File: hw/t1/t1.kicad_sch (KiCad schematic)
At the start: 65 parts, among them J1 SFP edge (INF-8074i), J2 Rosenberger E6S20A-40MT5-Z (H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, U1 DP83TG720S-Q1 (or DP83TC812S-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, U2 STM32G031F6P6, U3 TPS62822DLC, U4 TPS22918DBVR, Y1 25MHz CL8pF 2016

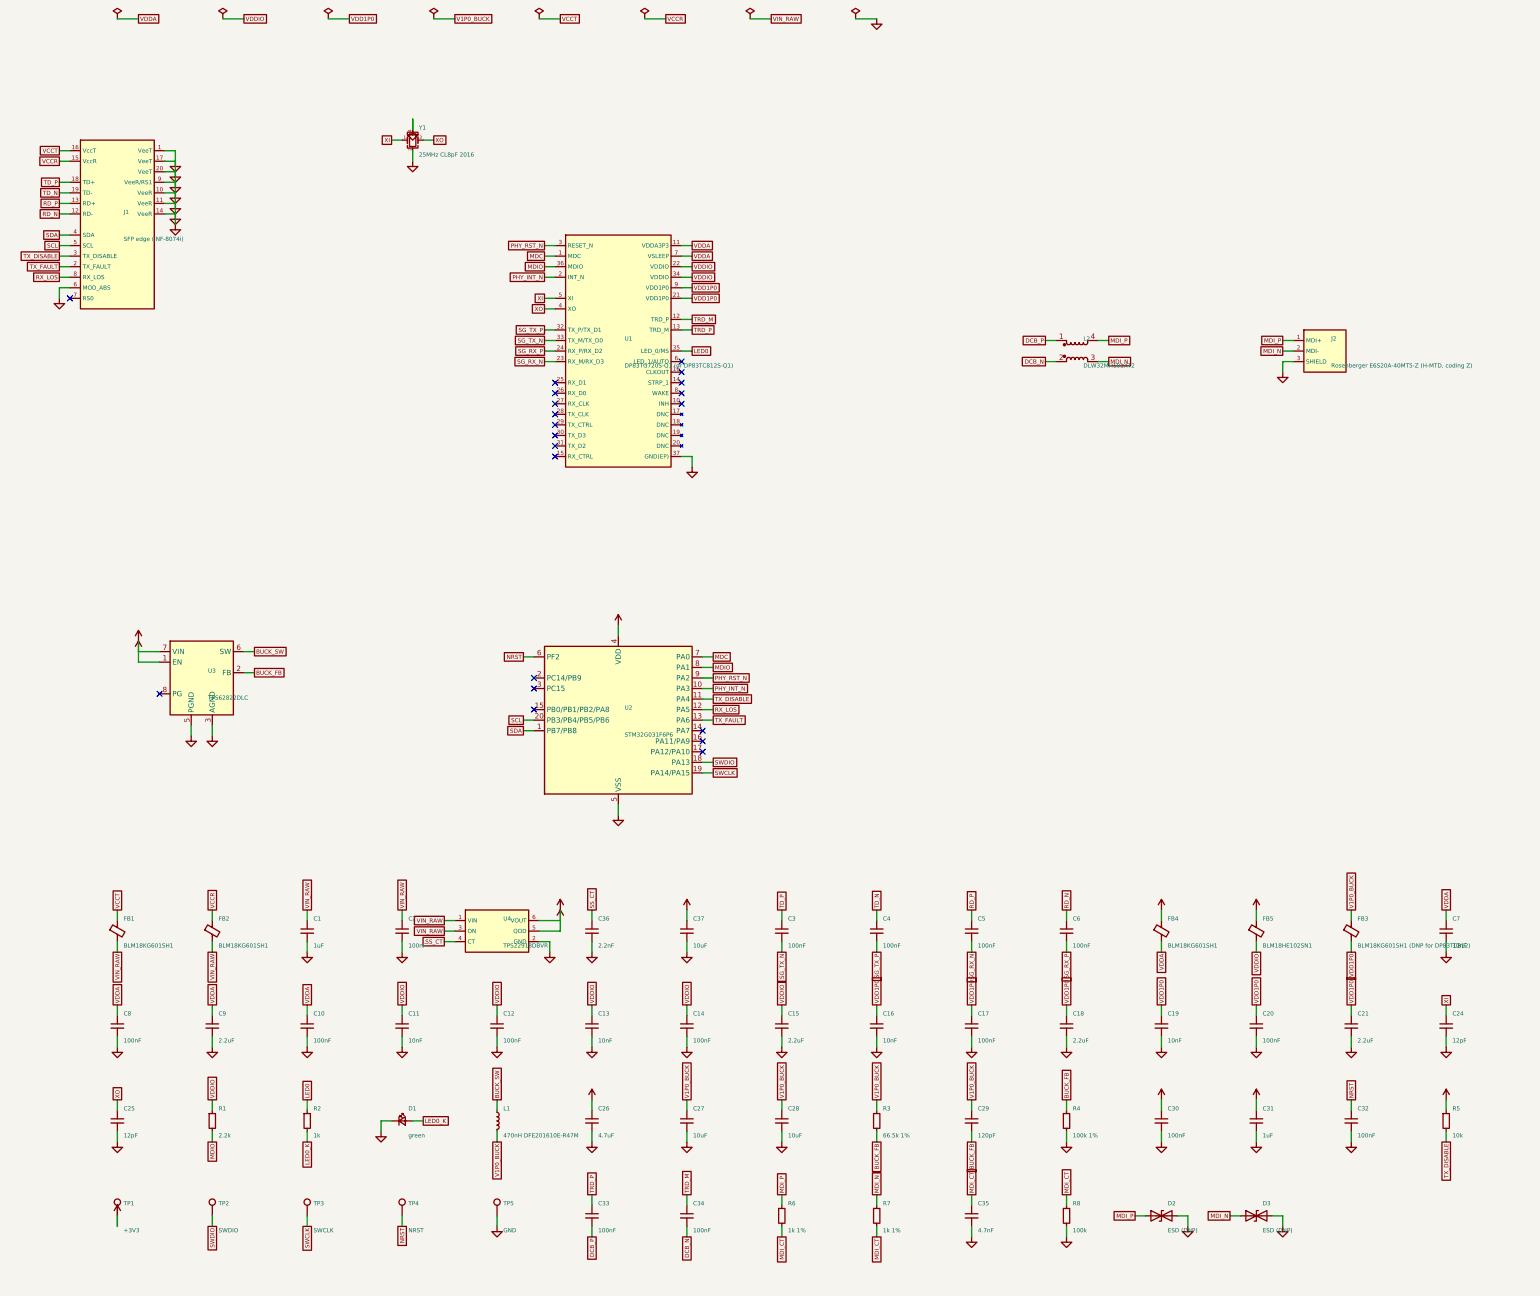
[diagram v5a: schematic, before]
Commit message: T1S: 6-layer board routed and clean, JLC panel and order sheet
- DRC 0 / 0 unconnected (KiCad 7 and 9), schematic parity clean, ERC 0
  errors; gerbers, BOM/CPL, 1:1 print; 5-board panel, DRC clean with the
  board's rules
- the core rail is an In4 island (on In2 it walled the ball field in); In2
  carries two hand-laid buses to the MCU, found once by a maze search and
  baked into make_t1s.py (IN2_BUS)
- JTAG pads beside the FPGA, flash turned 180 degrees, strap/XTO/+3V3 vias in
  the PHY's pads, the MDI pair swapped at the PHY (DME is polarity-free),
  L3/M12 reconnected (they had slipped into a comment)
- MCU pins follow the buses: TX_DISABLE / TX_FAULT on PC14 / PC15 (fw)
- sfpgen: side-pin power stubs no longer turn (GND on TXCLK merged half
  the FPGA's nets in the schematic); ISLANDS as outlines; router vias that
  double a plane dogbone are dropped; T1/RJ45 schematics regenerated,
  both still pass ERC and KiCad 9
- CI: t1s joins the KiCad 9 matrix
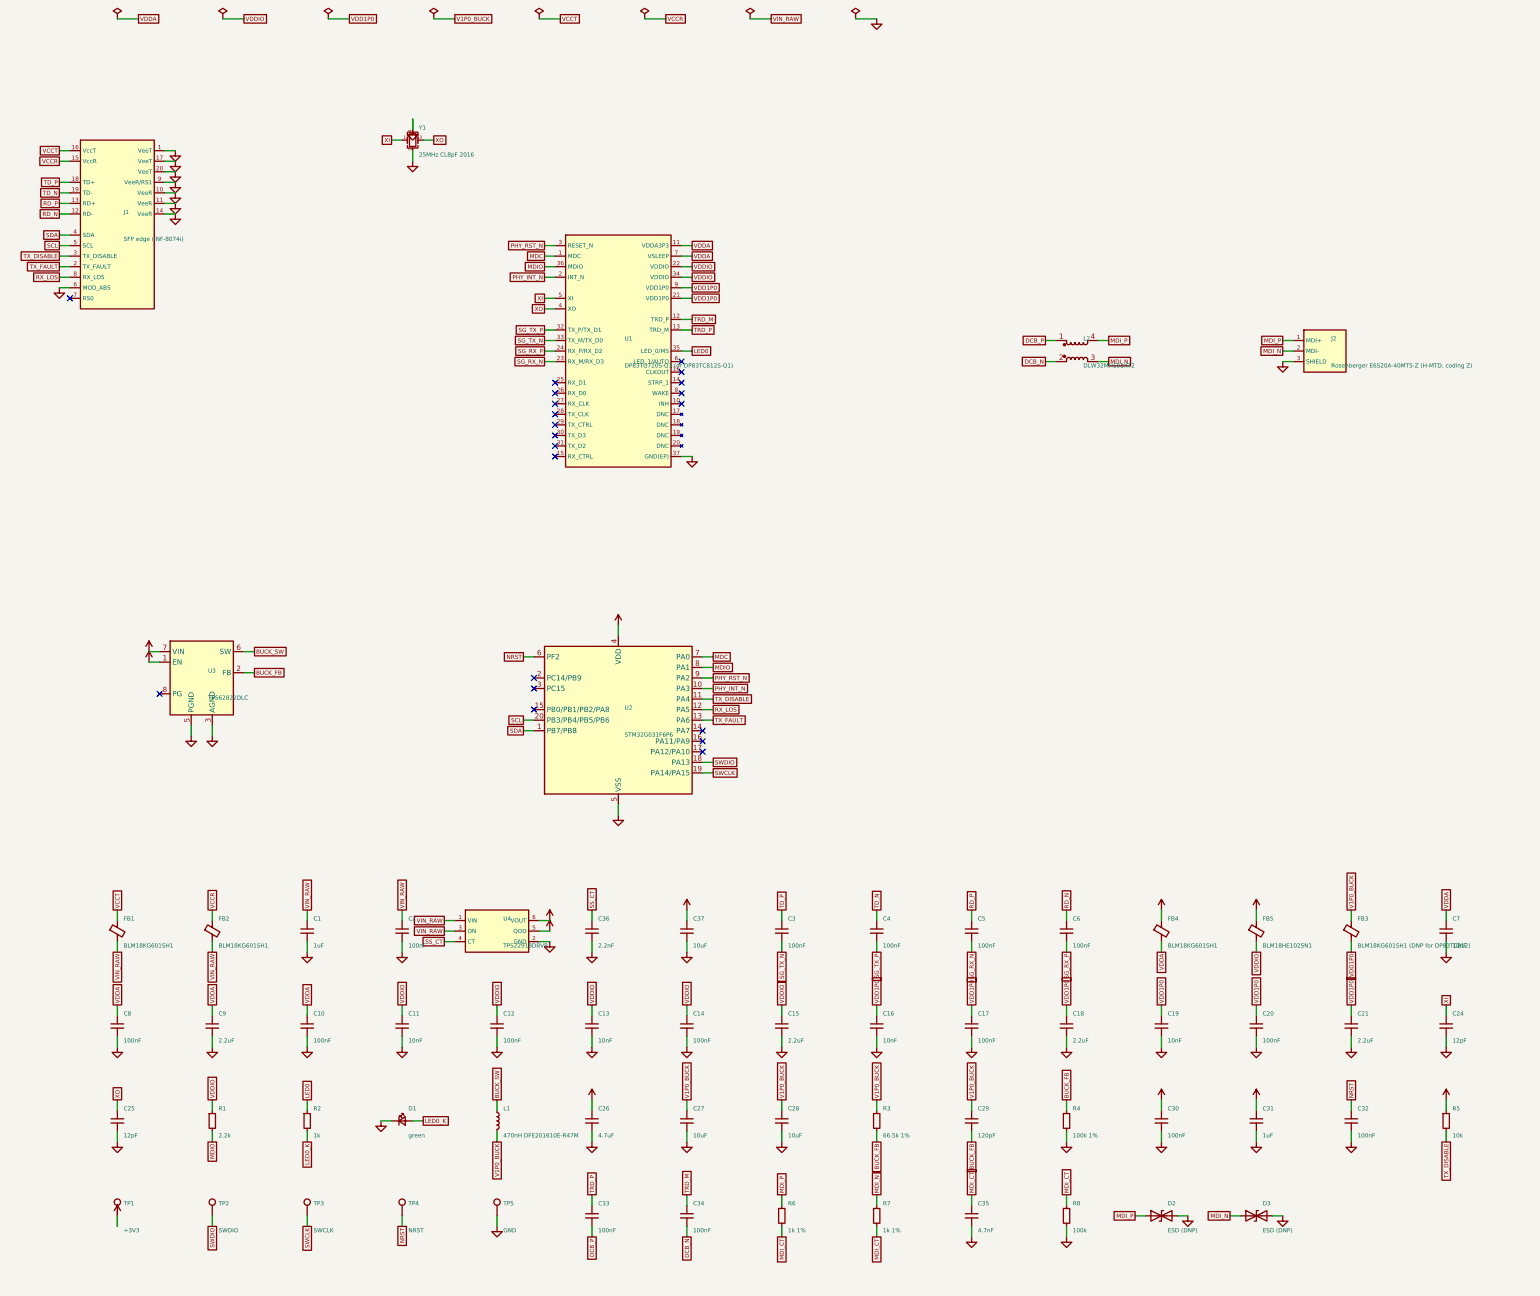
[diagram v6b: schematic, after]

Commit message: Review fixes: 100 V MDI DC block, 128 Mbit flash, T1S MDI geometry
- T1 C33/C34: 100 nF 100 V X5R 0402 (GRM155R62A104KE14D, C162178), split
  from the 16 V decap line (C1525) they had been grouped with
- T1 R6/R7: 1 k 1 % 0.2 W anti-surge 0402 (C313354) instead of 62.5 mW;
  still short of TI's 0.75 W 2010, documented
- T1S U2: GD25Q128EWIGR (C2982923), same WSON-8 footprint, so Gowin's
  default golden address 0x800000 is inside the part; ORDER.md gives the
  flash layout
- compliance.py: each lane's geometry comes from its routed track width;
  the T1S MDI is two 0.2 mm lines (Z0 44.8) with its own delay and loss,
  and an unsolved width now stops the run
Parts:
- C33, C34: value 100nF -> 100nF 100V; LCSC C1525 -> C162178; MPN (none) -> GRM155R62A104KE14D
- R6, R7: value 1k 1% -> 1k 1% 0.2W; LCSC C11702 -> C313354; MPN (none) -> CRCW04021K00FKEDHP
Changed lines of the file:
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@@
     (in_bom yes) (on_board yes) (dnp no)
     (property "Reference" "C33" (at 155.17 315.77 0) (effects (font (size 1.0 1.0)) (justify left)))
-    (property "Value" "100nF" (at 155.17 322.27 0) (effects (font (size 1.0 1.0)) (justify left)))
+    (property "Value" "100nF 100V" (at 155.17 322.27 0) (effects (font (size 1.0 1.0)) (justify left)))
     (property "Footprint" "Capacitor_SMD:C_0402_1005Metric" (at 153.67 318.77 0) (effects (font (size 1.0 1.0)) hide))
     (property "Datasheet" "" (at 153.67 318.77 0) (effects (font (size 1.0 1.0)) hide))
-    (property "LCSC" "C1525" (at 153.67 318.77 0) (effects (font (size 1.0 1.0)) hide))
+    (property "MPN" "GRM155R62A104KE14D" (at 153.67 318.77 0) (effects (font (size 1.0 1.0)) hide))
+    (property "LCSC" "C162178" (at 153.67 318.77 0) (effects (font (size 1.0 1.0)) hide))
     (pin "1")
     (pin "2")
@@
     (in_bom yes) (on_board yes) (dnp no)
     (property "Reference" "C34" (at 178.03 315.77 0) (effects (font (size 1.0 1.0)) (justify left)))
-    (property "Value" "100nF" (at 178.03 322.27 0) (effects (font (size 1.0 1.0)) (justify left)))
+    (property "Value" "100nF 100V" (at 178.03 322.27 0) (effects (font (size 1.0 1.0)) (justify left)))
     (property "Footprint" "Capacitor_SMD:C_0402_1005Metric" (at 176.53 318.77 0) (effects (font (size 1.0 1.0)) hide))
     (property "Datasheet" "" (at 176.53 318.77 0) (effects (font (size 1.0 1.0)) hide))
-    (property "LCSC" "C1525" (at 176.53 318.77 0) (effects (font (size 1.0 1.0)) hide))
+    (property "MPN" "GRM155R62A104KE14D" (at 176.53 318.77 0) (effects (font (size 1.0 1.0)) hide))
+    (property "LCSC" "C162178" (at 176.53 318.77 0) (effects (font (size 1.0 1.0)) hide))
     (pin "1")
     (pin "2")
@@
     (in_bom yes) (on_board yes) (dnp no)
     (property "Reference" "R6" (at 200.89 315.77 0) (effects (font (size 1.0 1.0)) (justify left)))
-    (property "Value" "1k 1%" (at 200.89 322.27 0) (effects (font (size 1.0 1.0)) (justify left)))
+    (property "Value" "1k 1% 0.2W" (at 200.89 322.27 0) (effects (font (size 1.0 1.0)) (justify left)))
     (property "Footprint" "Resistor_SMD:R_0402_1005Metric" (at 199.39 318.77 0) (effects (font (size 1.0 1.0)) hide))
     (property "Datasheet" "" (at 199.39 318.77 0) (effects (font (size 1.0 1.0)) hide))
-    (property "LCSC" "C11702" (at 199.39 318.77 0) (effects (font (size 1.0 1.0)) hide))
+    (property "MPN" "CRCW04021K00FKEDHP" (at 199.39 318.77 0) (effects (font (size 1.0 1.0)) hide))
+    (property "LCSC" "C313354" (at 199.39 318.77 0) (effects (font (size 1.0 1.0)) hide))
     (pin "1")
     (pin "2")
@@
     (in_bom yes) (on_board yes) (dnp no)
     (property "Reference" "R7" (at 223.75 315.77 0) (effects (font (size 1.0 1.0)) (justify left)))
-    (property "Value" "1k 1%" (at 223.75 322.27 0) (effects (font (size 1.0 1.0)) (justify left)))
+    (property "Value" "1k 1% 0.2W" (at 223.75 322.27 0) (effects (font (size 1.0 1.0)) (justify left)))
     (property "Footprint" "Resistor_SMD:R_0402_1005Metric" (at 222.25 318.77 0) (effects (font (size 1.0 1.0)) hide))
     (property "Datasheet" "" (at 222.25 318.77 0) (effects (font (size 1.0 1.0)) hide))
-    (property "LCSC" "C11702" (at 222.25 318.77 0) (effects (font (size 1.0 1.0)) hide))
+    (property "MPN" "CRCW04021K00FKEDHP" (at 222.25 318.77 0) (effects (font (size 1.0 1.0)) hide))
+    (property "LCSC" "C313354" (at 222.25 318.77 0) (effects (font (size 1.0 1.0)) hide))
     (pin "1")
     (pin "2")
